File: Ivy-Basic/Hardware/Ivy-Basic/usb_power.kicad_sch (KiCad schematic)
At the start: 15 parts, among them IC1 SSP9451, J1 USB_C_Receptacle_USB2.0_16P

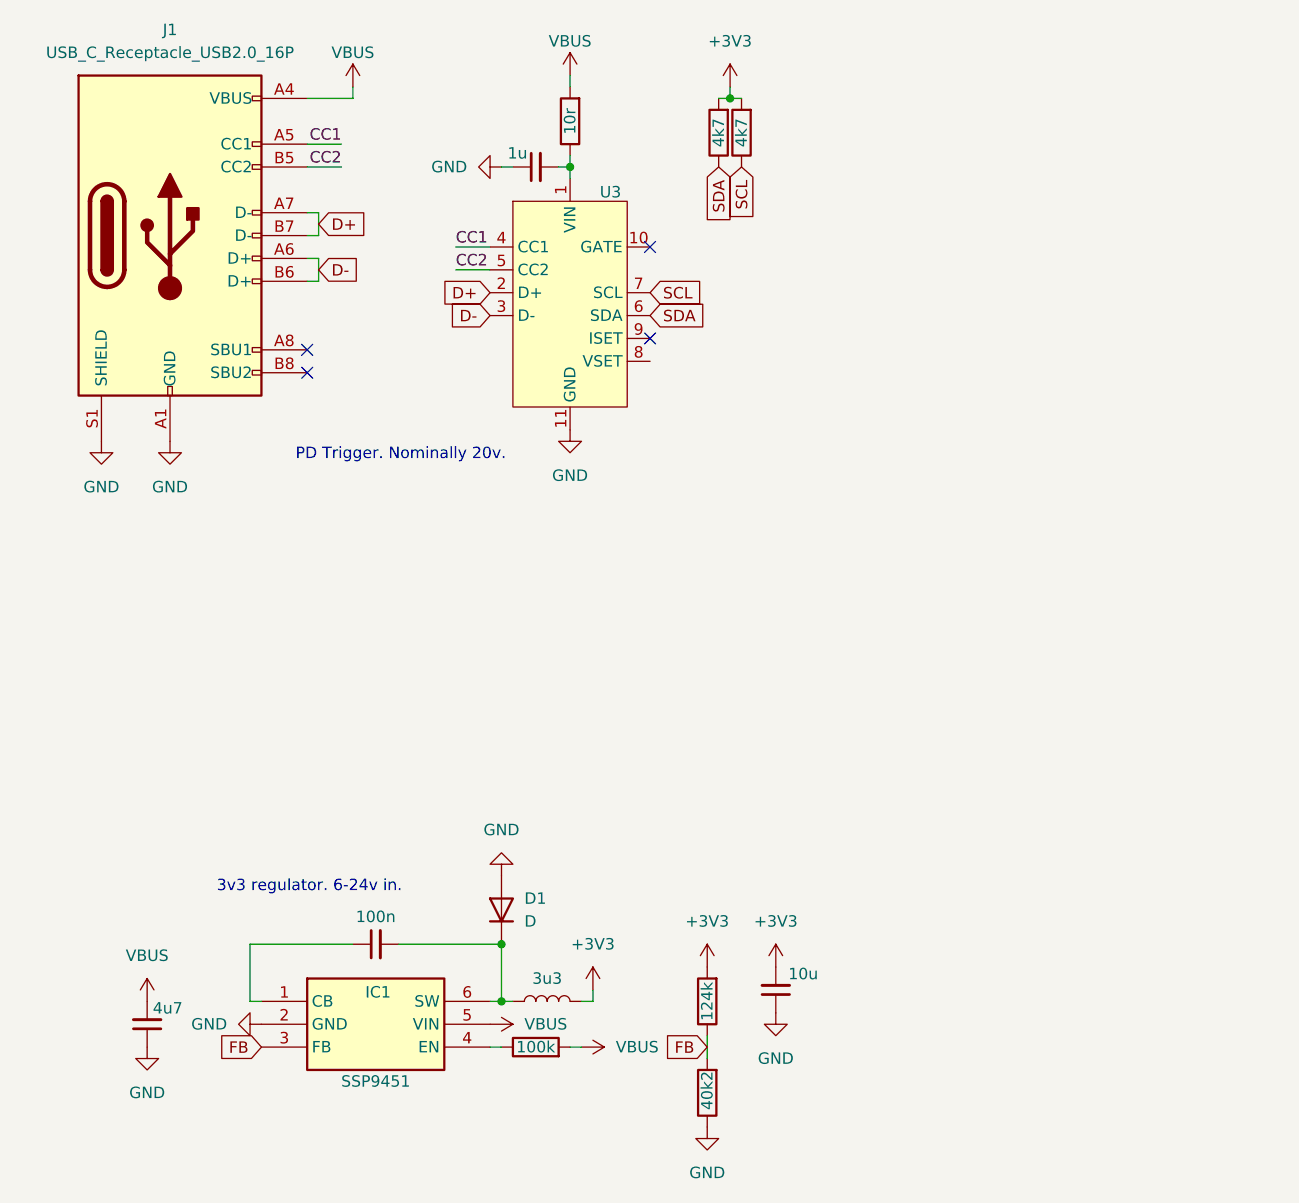
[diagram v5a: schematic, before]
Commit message: add TMC2209
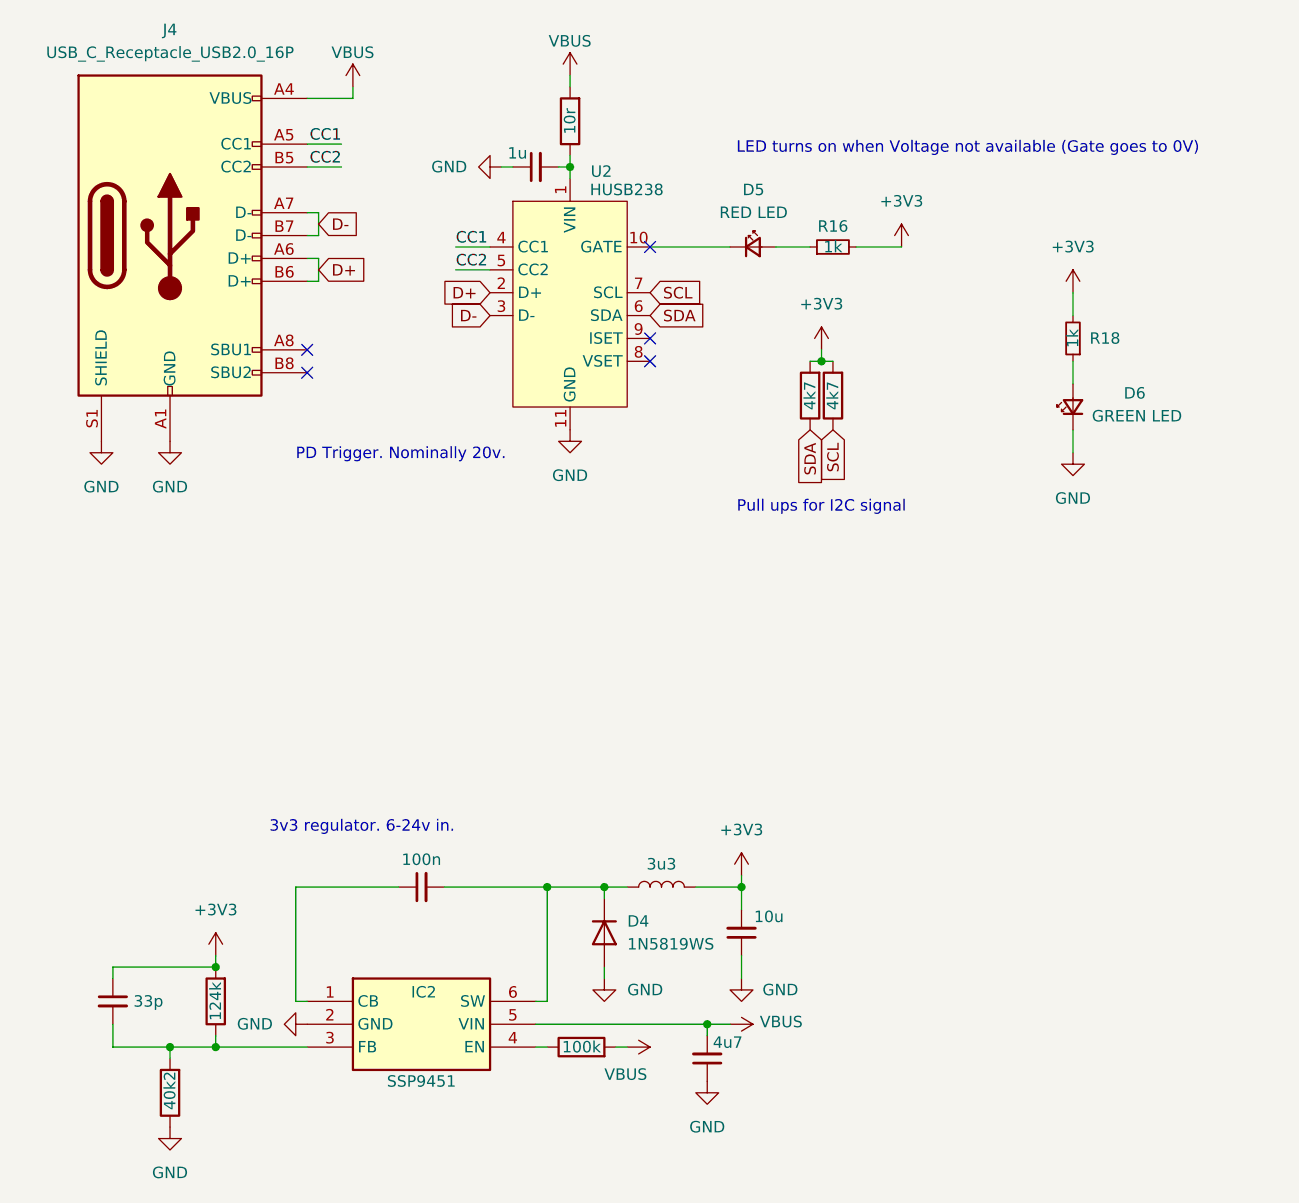
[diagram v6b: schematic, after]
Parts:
- added C15: 33p, Capacitor_SMD:C_0402_1005Metric, symbol Device:C_Small
- added D5: RED LED, LED_SMD:LED_0402_1005Metric, symbol Device:LED_Small
- added D6: GREEN LED, LED_SMD:LED_0402_1005Metric, symbol Device:LED_Small
- added R16, R18: 1k, Resistor_SMD:R_0402_1005Metric, symbol Device:R_Small
- D4: renamed from D1; value D -> 1N5819WS; LCSC (none) -> C191023
- U2: renamed from U3; value ~ -> HUSB238
- renumbered C10 to C16, C1 to C17, C11 to C18, C12 to C19, IC1 to IC2, J1 to J4, R6 to R11, R5 to R12, R1 to R13, R10 to R14, R2 to R15, R3 to R17
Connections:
- net +3V3: now also C15.1, R16.2, R18.2
- net D+: now also J4.A6 (D+), J4.B6 (D+); no longer J4.A7 (D-), J4.B7 (D-)
- net D-: now also J4.A7 (D-), J4.B7 (D-); no longer J4.A6 (D+), J4.B6 (D+)
- net GND: now also D6.1 (K)
- net at U2.10 (GATE): now also D5.1 (K)
- net FB: no longer names the net of IC2.3 (FB), R11.2, R12.1
- net FB: now also C15.2
- new net: D5.2 (A), R16.1
- new net: D6.2 (A), R18.1
- no-connect marks 4 -> 5
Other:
- note added: "LED turns on when Voltage not available (Gate goes to 0V)"
- note added: "Pull ups for I2C signal"
- moved on the sheet: D4, IC2
